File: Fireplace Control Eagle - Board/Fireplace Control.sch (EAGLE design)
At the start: 11 parts, among them IC2 MEGA8-PU, J1 POWER_JACKPTH, K1 AQV21SOP

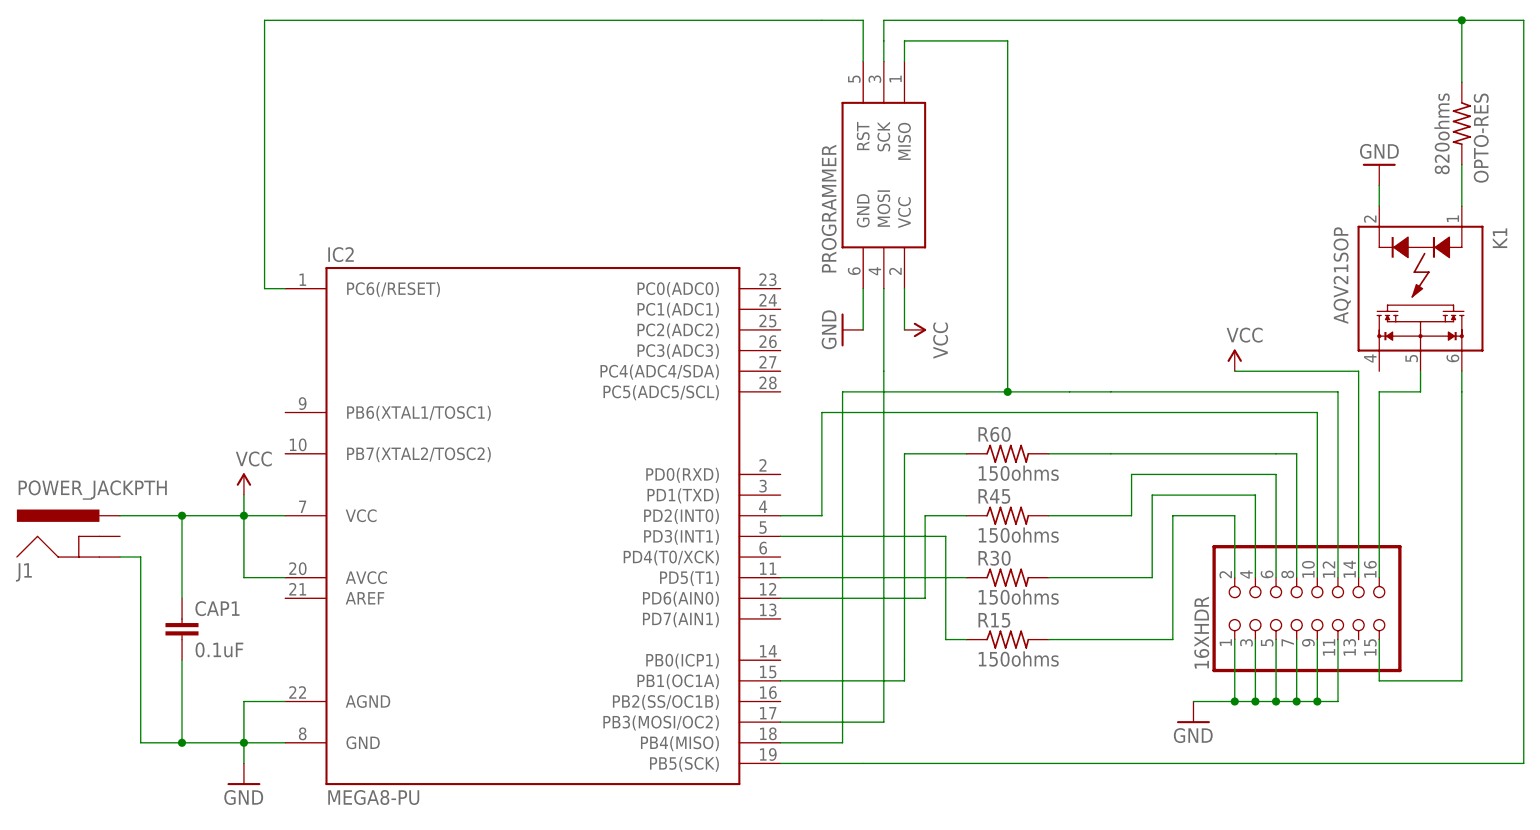
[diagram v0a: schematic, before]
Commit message: Submitted to OSHPark
This is the design that went to OSHPark for productions
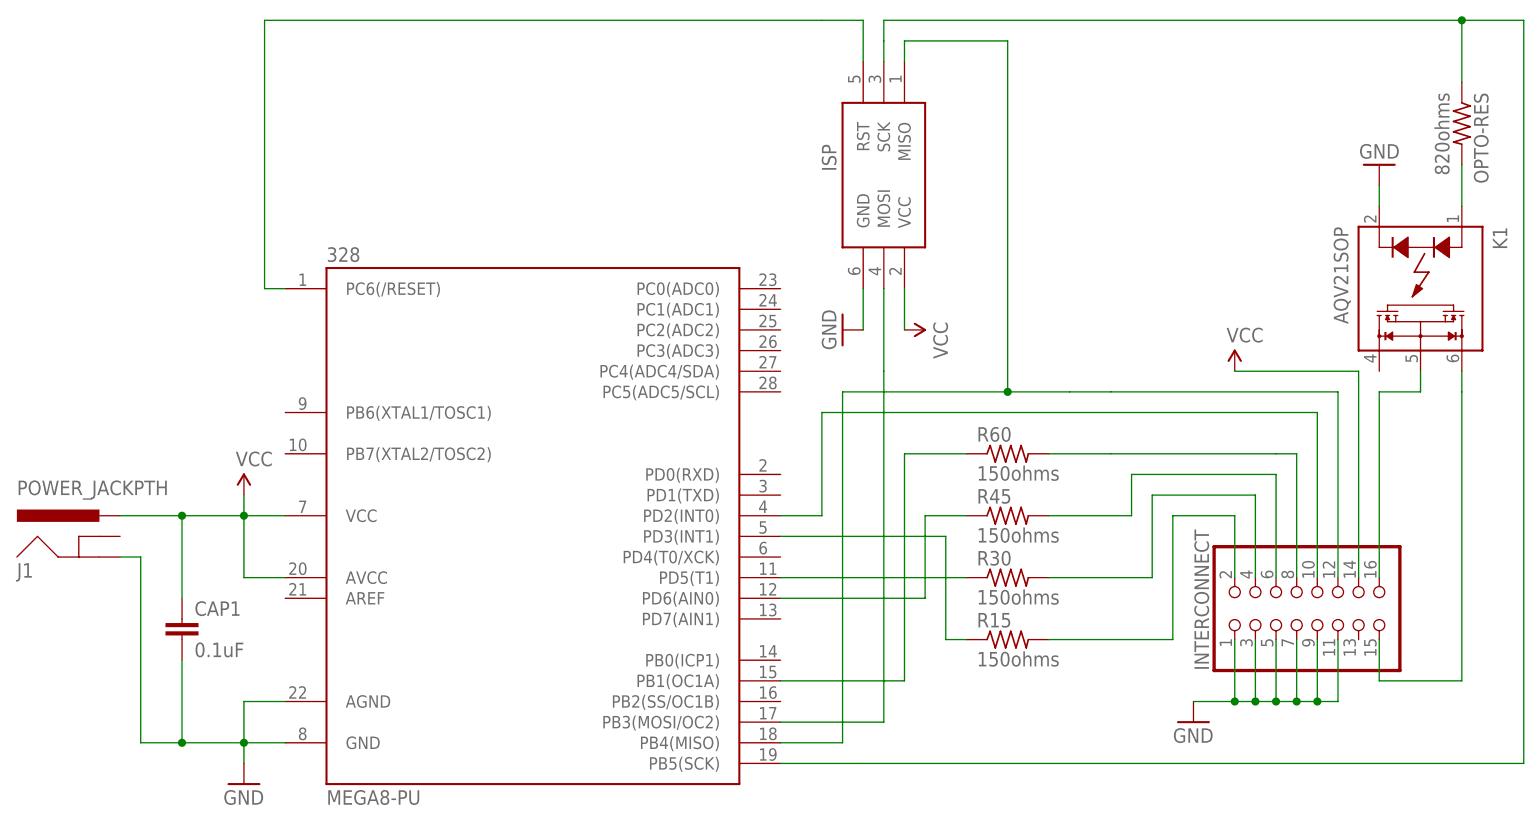
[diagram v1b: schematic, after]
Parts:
- renumbered 16XHDR to INTERCONNECT, IC2 to 328, PROGRAMMER to ISP

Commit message: First cut v2 Board
Rewired led60 to use pin 11 (instead of 9). Re-routed using FreeRoute
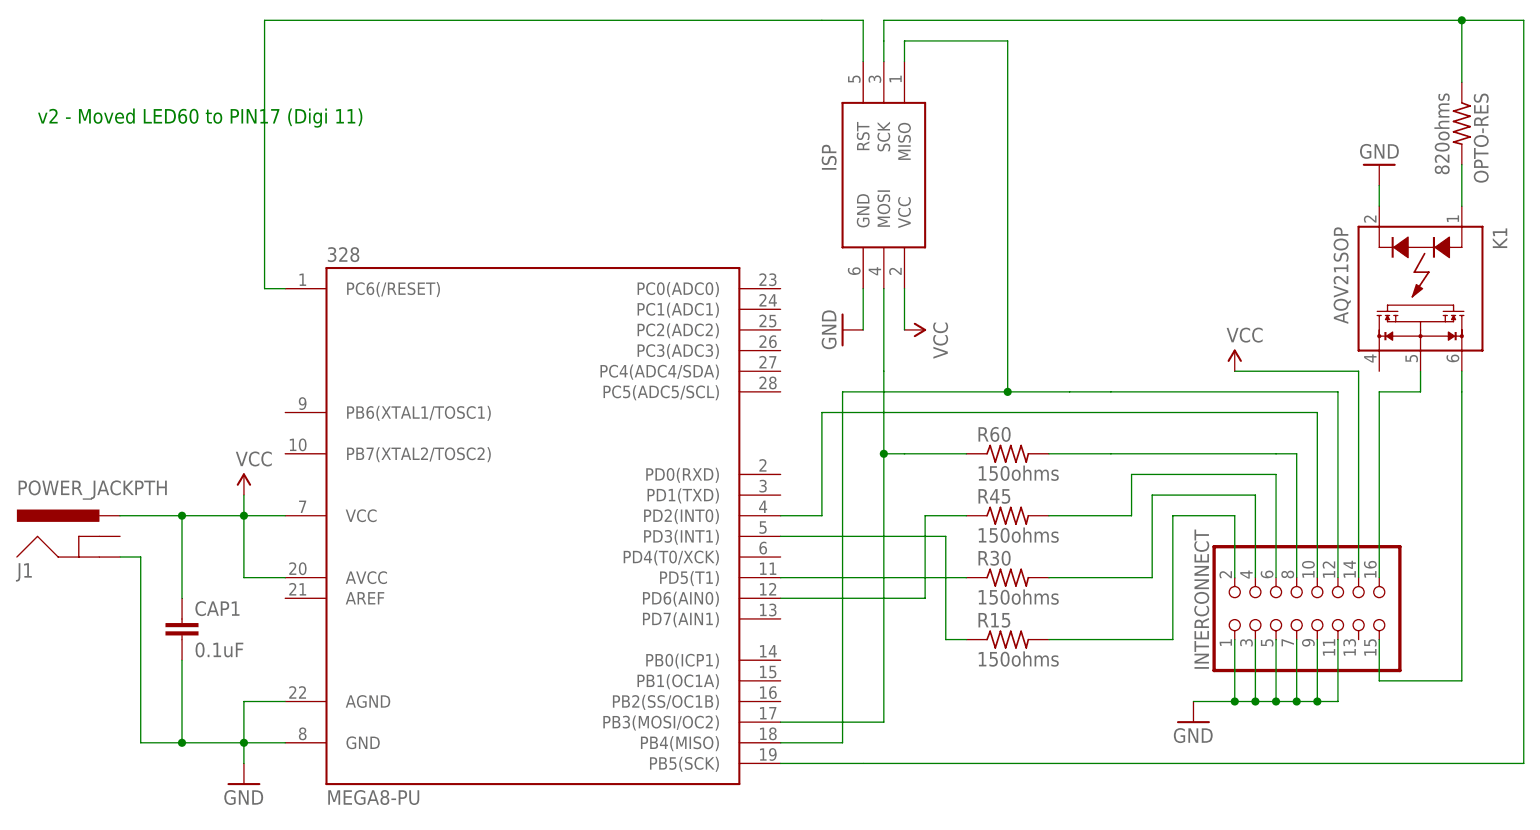
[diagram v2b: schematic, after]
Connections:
- removed net N$10: 328.PB3(MOSI/OC2), ISP.MOSI
- net N$8: now also 328.PB3(MOSI/OC2), ISP.MOSI; no longer 328.PB1(OC1A)
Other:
- note added: "v2 - Moved LED60 to PIN17 (Digi 11)"
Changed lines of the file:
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@@
 <sheet>
 <plain>
+<text x="-109.22" y="68.58" size="1.778" layer="91">v2 - Moved LED60 to PIN17 (Digi 11)</text>
 </plain>
 <instances>
@@
 <net name="N$8" class="0">
 <segment>
-<wire x1="-2.54" y1="2.54" x2="-2.54" y2="27.94" width="0.1524" layer="91"/>
 <wire x1="-2.54" y1="27.94" x2="5.08" y2="27.94" width="0.1524" layer="91"/>
 <pinref part="R60" gate="G$1" pin="1"/>
-<pinref part="328" gate="1" pin="PB1(OC1A)"/>
-<wire x1="-17.78" y1="0" x2="-2.54" y2="0" width="0.1524" layer="91"/>
-<wire x1="-2.54" y1="0" x2="-2.54" y2="2.54" width="0.1524" layer="91"/>
+<pinref part="ISP" gate="G$1" pin="MOSI"/>
+<pinref part="328" gate="1" pin="PB3(MOSI/OC2)"/>
+<wire x1="-17.78" y1="-5.08" x2="-5.08" y2="-5.08" width="0.1524" layer="91"/>
+<wire x1="-5.08" y1="-5.08" x2="-5.08" y2="27.94" width="0.1524" layer="91"/>
+<wire x1="-5.08" y1="27.94" x2="-5.08" y2="38.1" width="0.1524" layer="91"/>
+<wire x1="-5.08" y1="48.26" x2="-5.08" y2="38.1" width="0.1524" layer="91"/>
+<wire x1="-2.54" y1="27.94" x2="-5.08" y2="27.94" width="0.1524" layer="91"/>
+<junction x="-5.08" y="27.94"/>
 </segment>
 </net>
@@
 </segment>
 </net>
-<net name="N$10" class="0">
-<segment>
-<pinref part="ISP" gate="G$1" pin="MOSI"/>
-<pinref part="328" gate="1" pin="PB3(MOSI/OC2)"/>
-<wire x1="-17.78" y1="-5.08" x2="-5.08" y2="-5.08" width="0.1524" layer="91"/>
-<wire x1="-5.08" y1="-5.08" x2="-5.08" y2="38.1" width="0.1524" layer="91"/>
-<wire x1="-5.08" y1="48.26" x2="-5.08" y2="38.1" width="0.1524" layer="91"/>
-</segment>
-</net>
